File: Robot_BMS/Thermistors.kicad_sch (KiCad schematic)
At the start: 12 parts

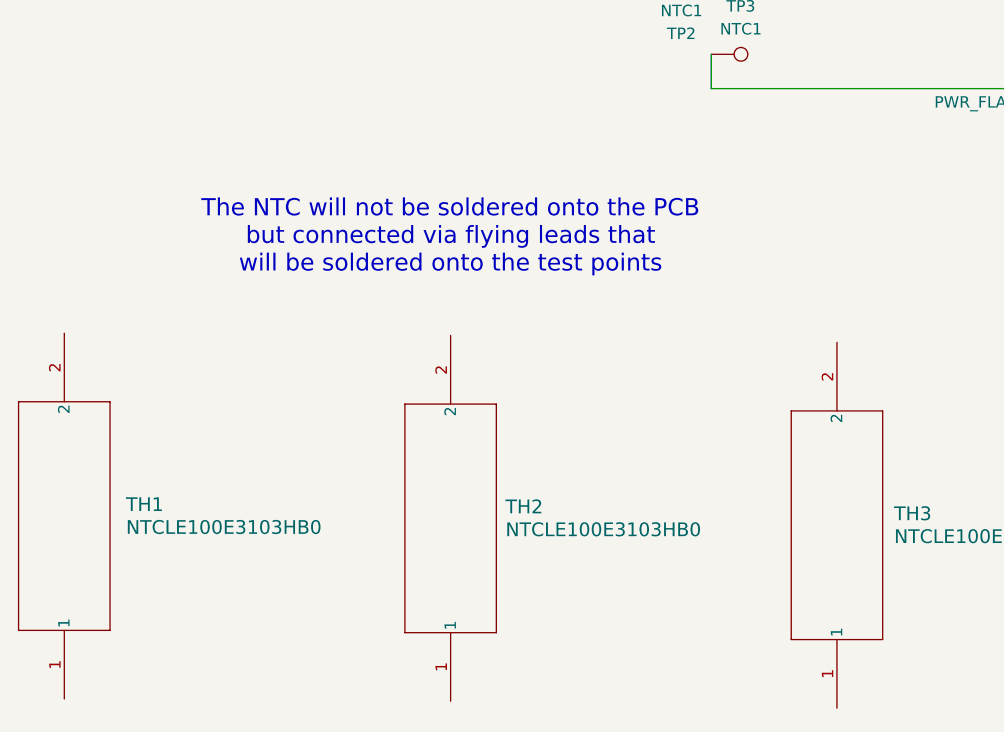
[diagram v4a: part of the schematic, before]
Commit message: still adding in symbols & footprints for passives
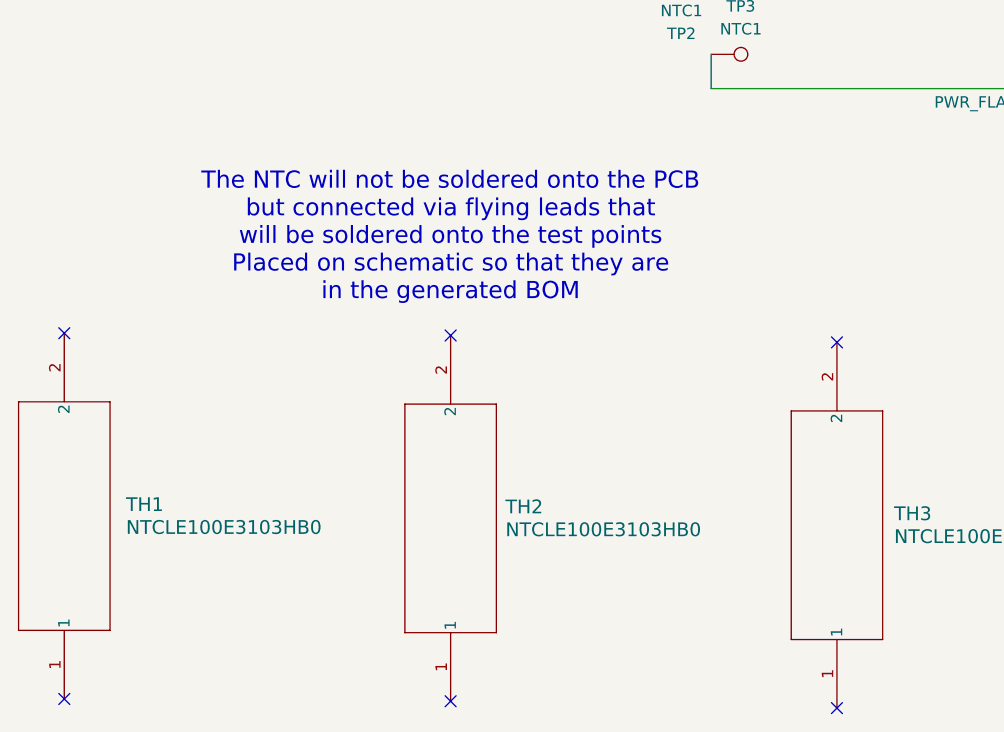
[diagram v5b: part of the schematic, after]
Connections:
- no-connect marks 0 -> 6
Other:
- note added: "The NTC will not be soldered onto the PCB but connected via flying leads that will be soldered onto the test points Placed on schematic so that they are in the generated BOM"
- note removed: "The NTC will not be soldered onto the PCB but connected via flying leads that will be soldered onto the test points"
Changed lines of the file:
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@@
 		(color 0 0 0 0)
+	)
+	(no_connect
+		(at 107.95 155.194)
+	)
+	(no_connect
+		(at 22.098 194.818)
+	)
+	(no_connect
+		(at 65.024 195.072)
+	)
+	(no_connect
+		(at 107.95 195.834)
+	)
+	(no_connect
+		(at 65.024 154.432)
+	)
+	(no_connect
+		(at 22.098 154.178)
 	)
 	(wire
@@
 		)
 	)
-	(text "The NTC will not be soldered onto the PCB\nbut connected via flying leads that\nwill be soldered onto the test points"
+	(text "The NTC will not be soldered onto the PCB\nbut connected via flying leads that\nwill be soldered onto the test points\nPlaced on schematic so that they are\nin the generated BOM"
 		(exclude_from_sim no)
 		(at 65.024 143.51 0)

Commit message: all symbols footprints & models added
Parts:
- renumbered R26 to R1, R3 to R2, R1 to R3, TP2 to TP1, TP3 to TP2, TP4 to TP3, TP5 to TP4, TP6 to TP5, TP7 to TP6
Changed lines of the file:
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@@
 		(on_board yes)
 		(dnp no)
-		(property "Reference" "TP6"
+		(property "Reference" "TP5"
 			(at 163.068 120.904 90)
 			(effects
@@
 			(project "Robot_BMS"
 				(path "/72551b1c-3d40-4199-8911-e5b015f4abec/cb04dfab-e035-4615-b482-7ed1936c63ff"
-					(reference "TP6")
+					(reference "TP5")
 					(unit 1)
 				)
@@
 		(on_board yes)
 		(dnp no)
-		(property "Reference" "TP3"
+		(property "Reference" "TP2"
 			(at 97.282 117.856 90)
 			(effects
@@
 			(project "Robot_BMS"
 				(path "/72551b1c-3d40-4199-8911-e5b015f4abec/cb04dfab-e035-4615-b482-7ed1936c63ff"
-					(reference "TP3")
+					(reference "TP2")
 					(unit 1)
 				)
@@
 		(on_board yes)
 		(dnp no)
-		(property "Reference" "TP4"
+		(property "Reference" "TP3"
 			(at 128.778 120.904 90)
 			(effects
@@
 			(project "Robot_BMS"
 				(path "/72551b1c-3d40-4199-8911-e5b015f4abec/cb04dfab-e035-4615-b482-7ed1936c63ff"
-					(reference "TP4")
+					(reference "TP3")
 					(unit 1)
 				)
@@
 		(on_board yes)
 		(dnp no)
-		(property "Reference" "TP5"
+		(property "Reference" "TP4"
 			(at 135.382 117.856 90)
 			(effects
@@
 			(project "Robot_BMS"
 				(path "/72551b1c-3d40-4199-8911-e5b015f4abec/cb04dfab-e035-4615-b482-7ed1936c63ff"
-					(reference "TP5")
+					(reference "TP4")
 					(unit 1)
 				)
@@
 		(on_board yes)
 		(dnp no)
-		(property "Reference" "TP2"
+		(property "Reference" "TP1"
 			(at 90.678 120.904 90)
 			(effects
@@
 			(project "Robot_BMS"
 				(path "/72551b1c-3d40-4199-8911-e5b015f4abec/cb04dfab-e035-4615-b482-7ed1936c63ff"
-					(reference "TP2")
+					(reference "TP1")
 					(unit 1)
 				)
@@
 		(on_board yes)
 		(dnp no)
-		(property "Reference" "TP7"
+		(property "Reference" "TP6"
 			(at 169.672 117.856 90)
 			(effects
@@
 			(project "Robot_BMS"
 				(path "/72551b1c-3d40-4199-8911-e5b015f4abec/cb04dfab-e035-4615-b482-7ed1936c63ff"
-					(reference "TP7")
+					(reference "TP6")
 					(unit 1)
 				)
@@
 		(on_board yes)
 		(dnp no)
-		(property "Reference" "R26"
+		(property "Reference" "R1"
 			(at 91.694 97.0279 90)
 			(effects
@@
 			(project ""
 				(path "/72551b1c-3d40-4199-8911-e5b015f4abec/cb04dfab-e035-4615-b482-7ed1936c63ff"
-					(reference "R26")
+					(reference "R1")
 					(unit 1)
 				)
@@
 		(on_board yes)
 		(dnp no)
-		(property "Reference" "R1"
+		(property "Reference" "R3"
 			(at 164.084 94.9959 90)
 			(effects
@@
 			(project "Robot_BMS"
 				(path "/72551b1c-3d40-4199-8911-e5b015f4abec/cb04dfab-e035-4615-b482-7ed1936c63ff"
-					(reference "R1")
+					(reference "R3")
 					(unit 1)
 				)
@@
 		(on_board yes)
 		(dnp no)
-		(property "Reference" "R3"
+		(property "Reference" "R2"
 			(at 129.794 96.5199 90)
 			(effects
@@
 			(project "Robot_BMS"
 				(path "/72551b1c-3d40-4199-8911-e5b015f4abec/cb04dfab-e035-4615-b482-7ed1936c63ff"
-					(reference "R3")
-					(unit 1)
-				)
+					(reference "R2")
+					(unit 1)
+				)

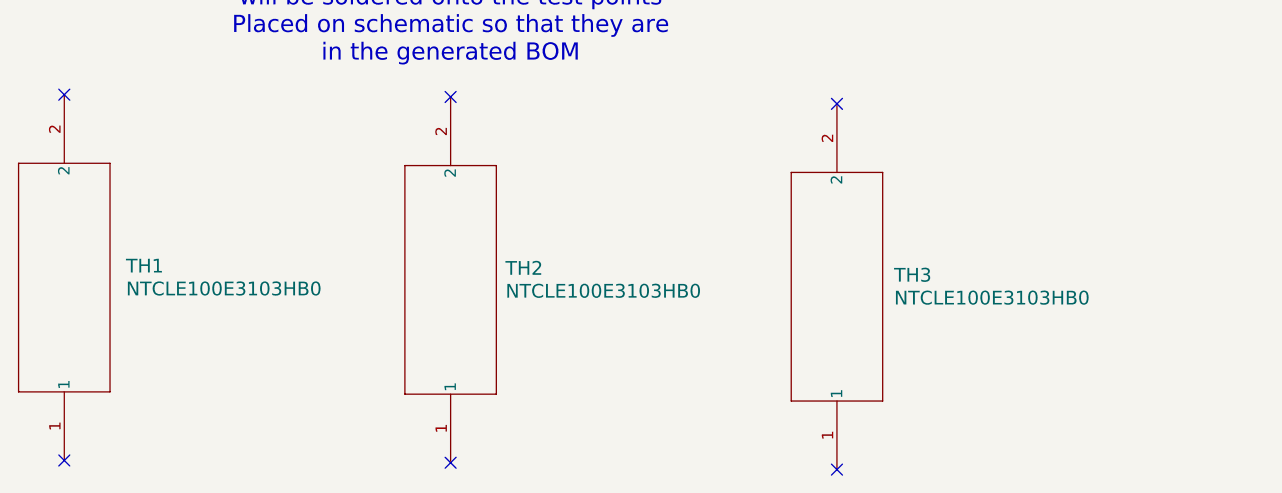
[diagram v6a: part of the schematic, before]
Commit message: BOM done, with total price £40
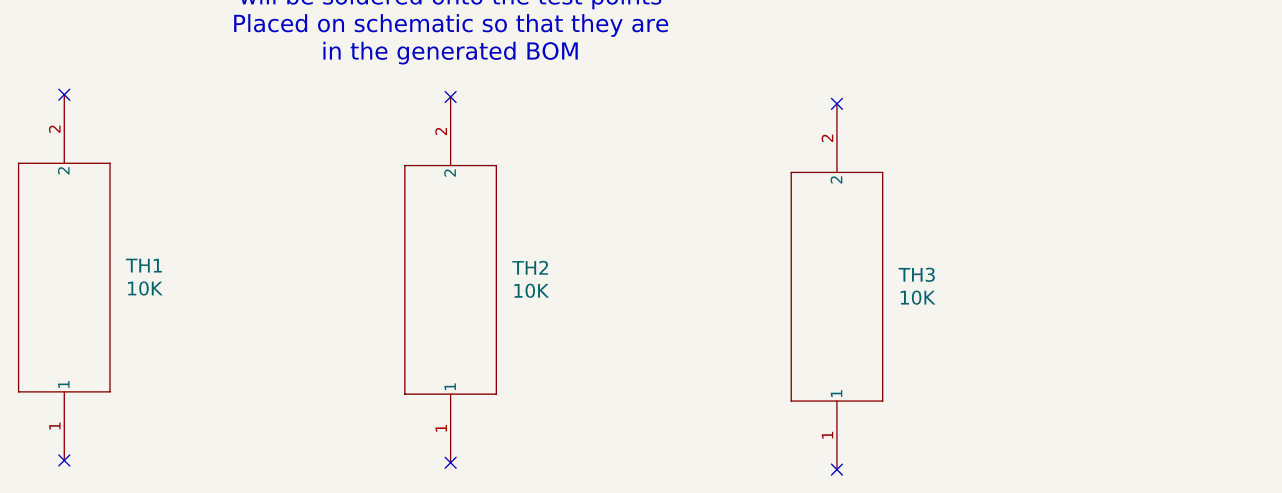
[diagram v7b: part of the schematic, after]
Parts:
- R1, R2, R3: Manufacturer_Part_Number (none) -> RC0603FR-073K24L; Price (none) -> 0.08
- TH1, TH2, TH3: value NTCLE100E3103HB0 -> 10K; Manufacturer_Part_Number (none) -> NTCLE100E3103HB0; Price (none) -> 0.45
- TP1, TP2, TP3, TP4, TP5, TP6: Manufacturer_Part_Number (none) -> exposed pad; Price (none) -> 0

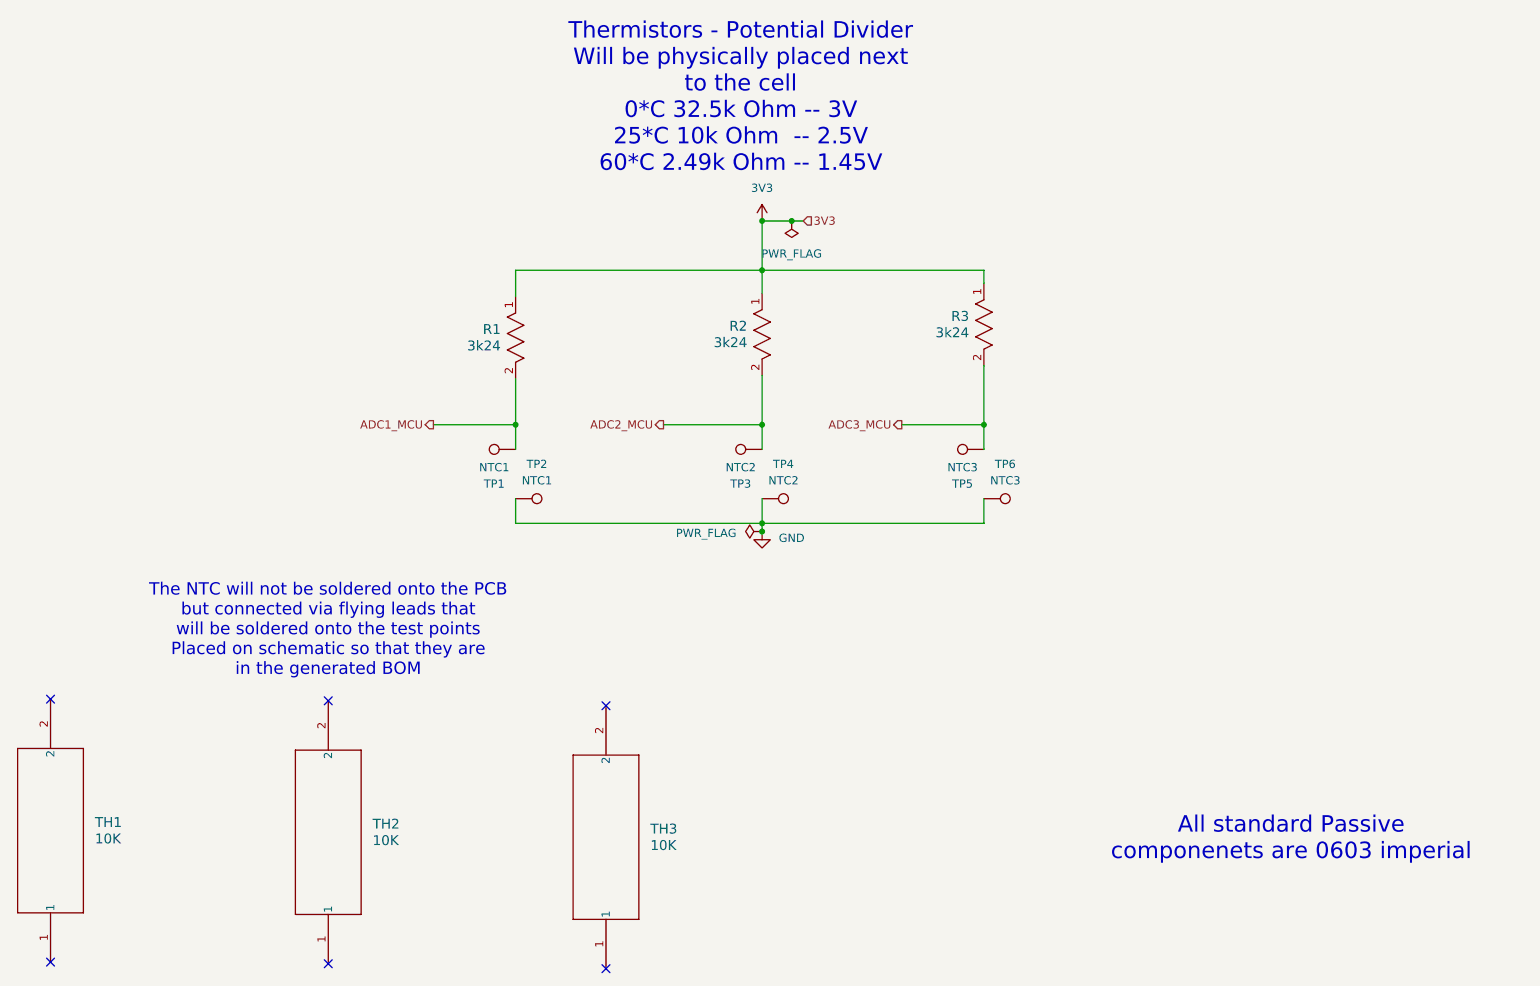
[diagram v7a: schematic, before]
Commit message: PCB layout up to charging circuit
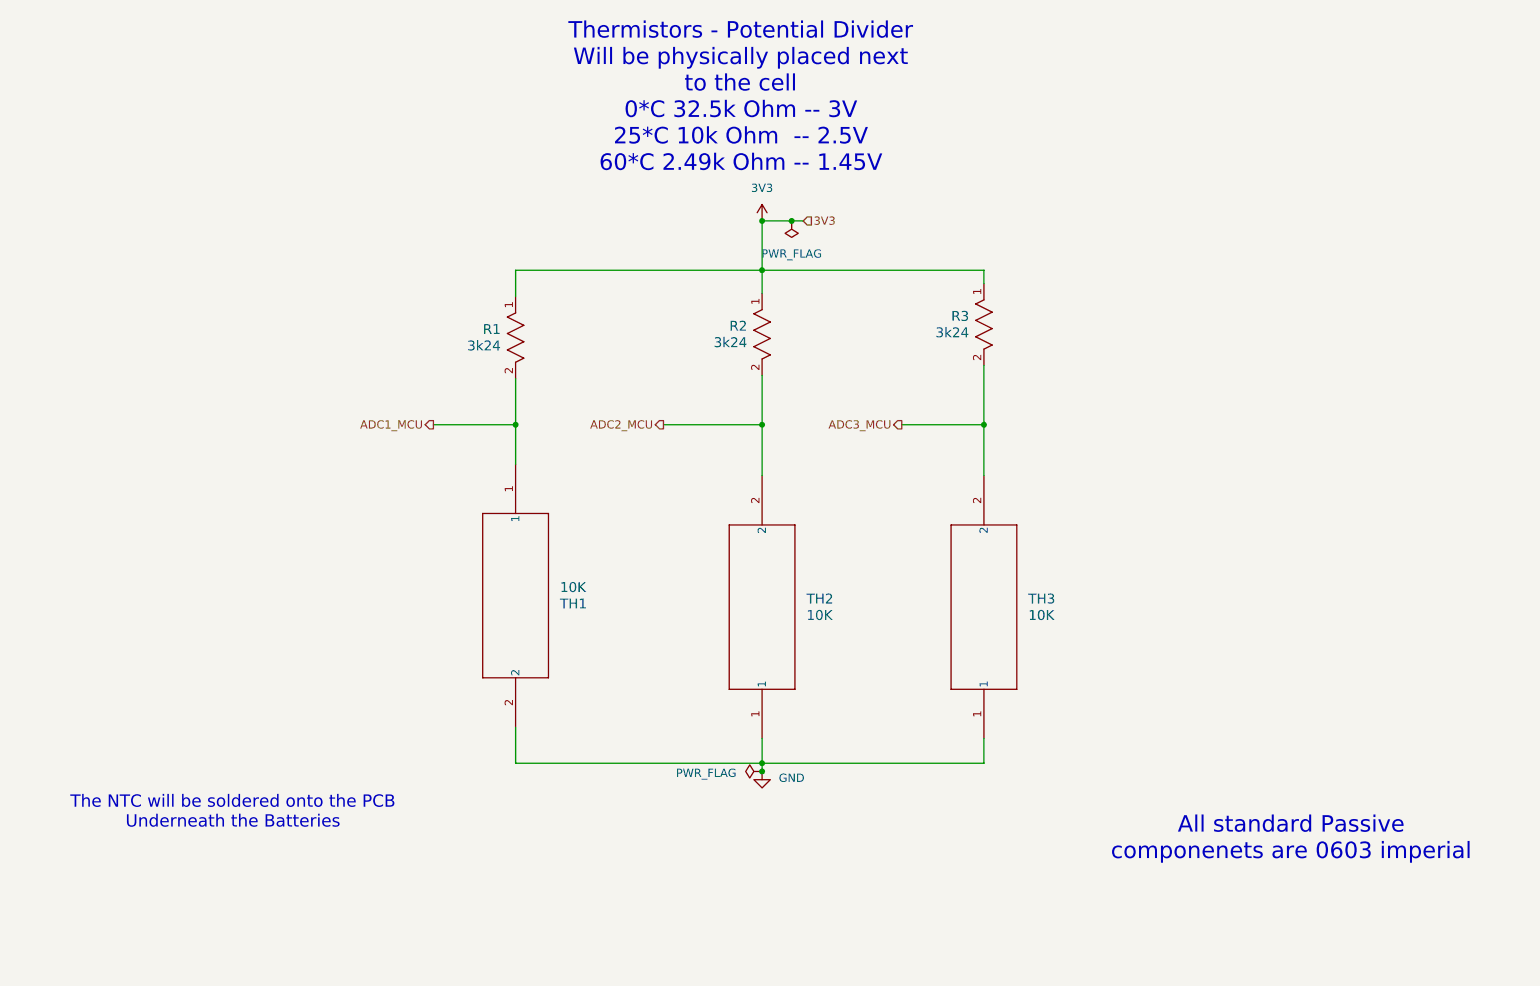
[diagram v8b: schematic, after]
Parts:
- removed TP1, TP2: NTC1, TestPoint:TestPoint_Pad_D4.0mm, symbol Connector:TestPoint
- removed TP3, TP4: NTC2, TestPoint:TestPoint_Pad_D4.0mm, symbol Connector:TestPoint
- removed TP5, TP6: NTC3, TestPoint:TestPoint_Pad_D4.0mm, symbol Connector:TestPoint
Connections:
- net ADC1_MCU: now also TH1.1
- net ADC2_MCU: now also TH2.2
- net ADC3_MCU: now also TH3.2
- net GND: now also TH1.2, TH2.1, TH3.1
- no-connect marks 6 -> 0
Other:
- note added: "The NTC will be soldered onto the PCB Underneath the Batteries"
- note removed: "The NTC will not be soldered onto the PCB but connected via flying leads that will be soldered onto the test points Placed on schematic so that they are in the generated BOM"
- moved on the sheet: TH1, TH2, TH3
